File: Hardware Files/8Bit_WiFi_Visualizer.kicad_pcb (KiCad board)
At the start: 2 copper layers, 59 x 44.5 mm, 34 parts, among them J1 USB_B_Micro, J2 Conn_01x04, SW1 SW_Push_Dual, SW2 SW_SPST, SW3 SW_SPST, U1 3.3V 1A, U2 74HC595, U3 ESP-WROOM-02D

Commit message: Update esp02 model on board
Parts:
- SW1: footprint PacketVis_Footprints:PTS645SK50SMTR92 LFS -> 8Bit_WiFi_Visualizer_Footprints:PTS645SK50SMTR92 LFS
- SW2, SW3: footprint PacketVis_Footprints:PTS636_SM25F_SMTR_LFS -> 8Bit_WiFi_Visualizer_Footprints:PTS636_SM25F_SMTR_LFS
- U3: footprint PacketVis_Footprints:ESP-WROOM-02D -> 8Bit_WiFi_Visualizer_Footprints:ESP-WROOM-02D

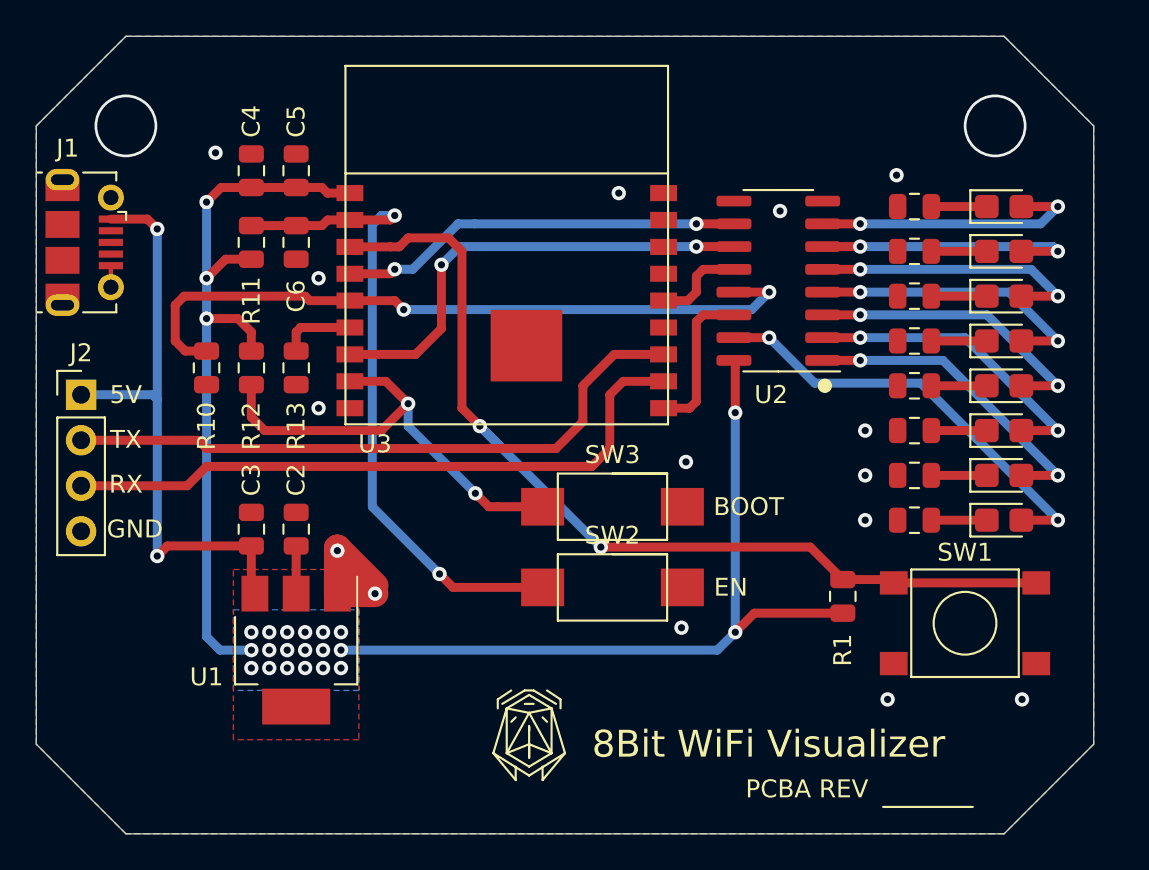
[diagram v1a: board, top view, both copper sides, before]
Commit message: Update microusb to include 3D model
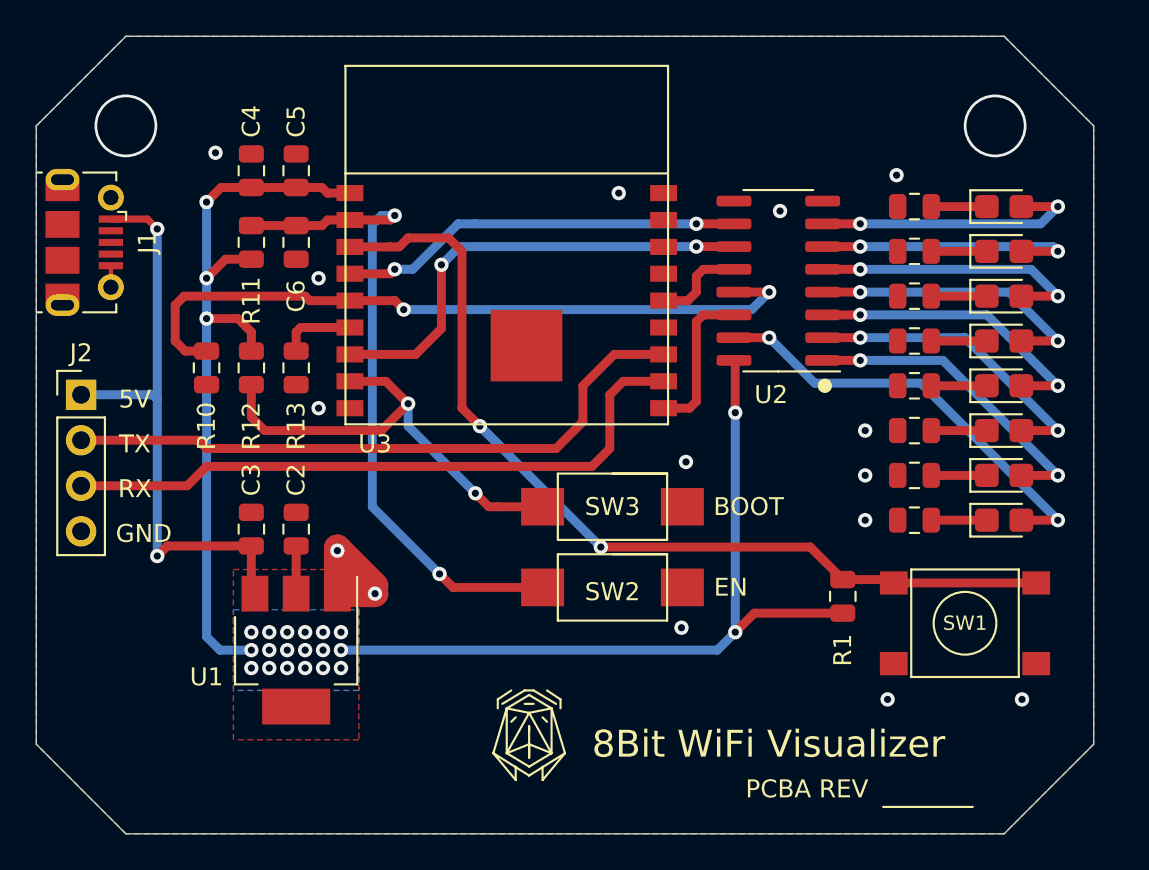
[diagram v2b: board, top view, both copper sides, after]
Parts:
- J1: footprint Connector_USB:USB_Micro-B_Molex-105017-0001 -> 8Bit_WiFi_Visualizer_Footprints:USB_Micro-B_Molex-105017-0001_3D
